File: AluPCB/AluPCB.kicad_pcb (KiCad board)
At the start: 2 copper layers, 60 x 50 mm, 78 parts, among them J1 CON_U, J2 CON_U, J3 CON_U, Q1 AON6276, Q2 AON6276, Q3 AON6276, Q4 AON6276, Q5 AON6276, Q6 AON6276

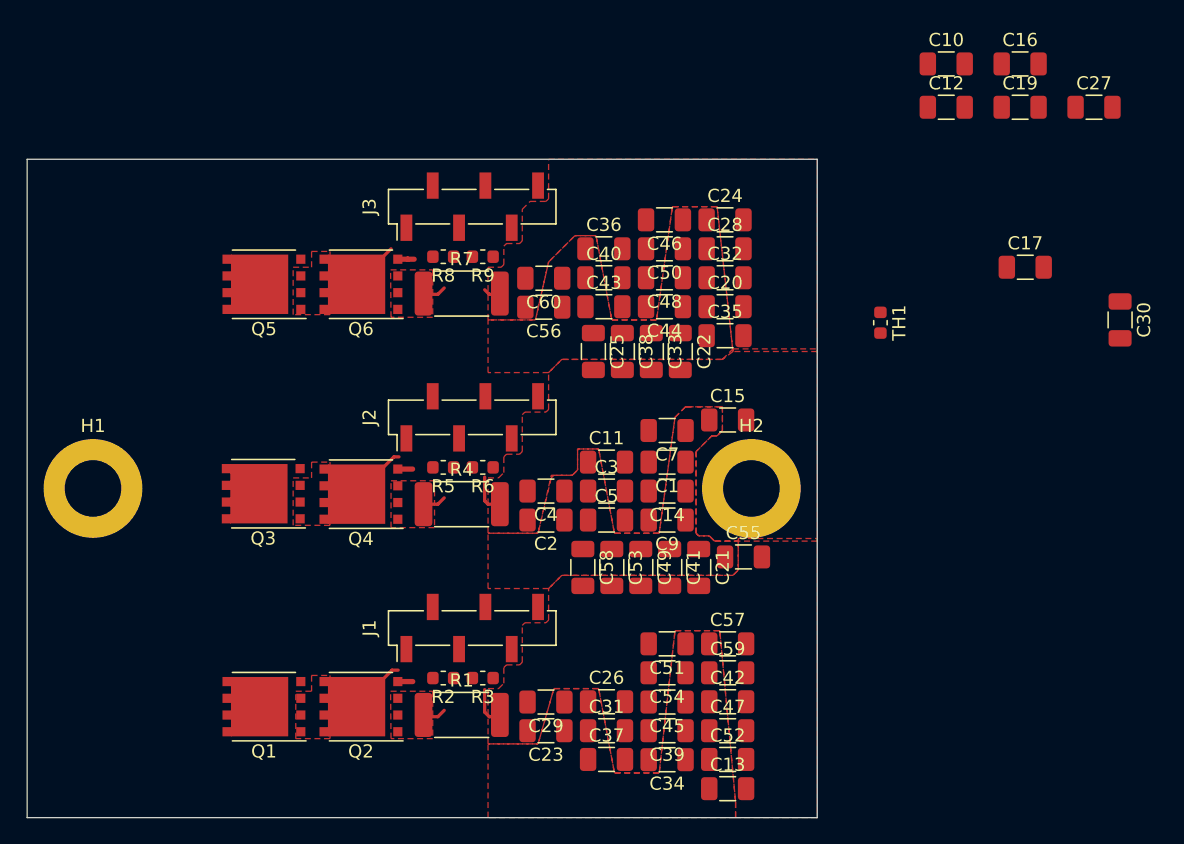
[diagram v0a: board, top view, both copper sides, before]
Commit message: finished AluPCB Power Stage 1, added images
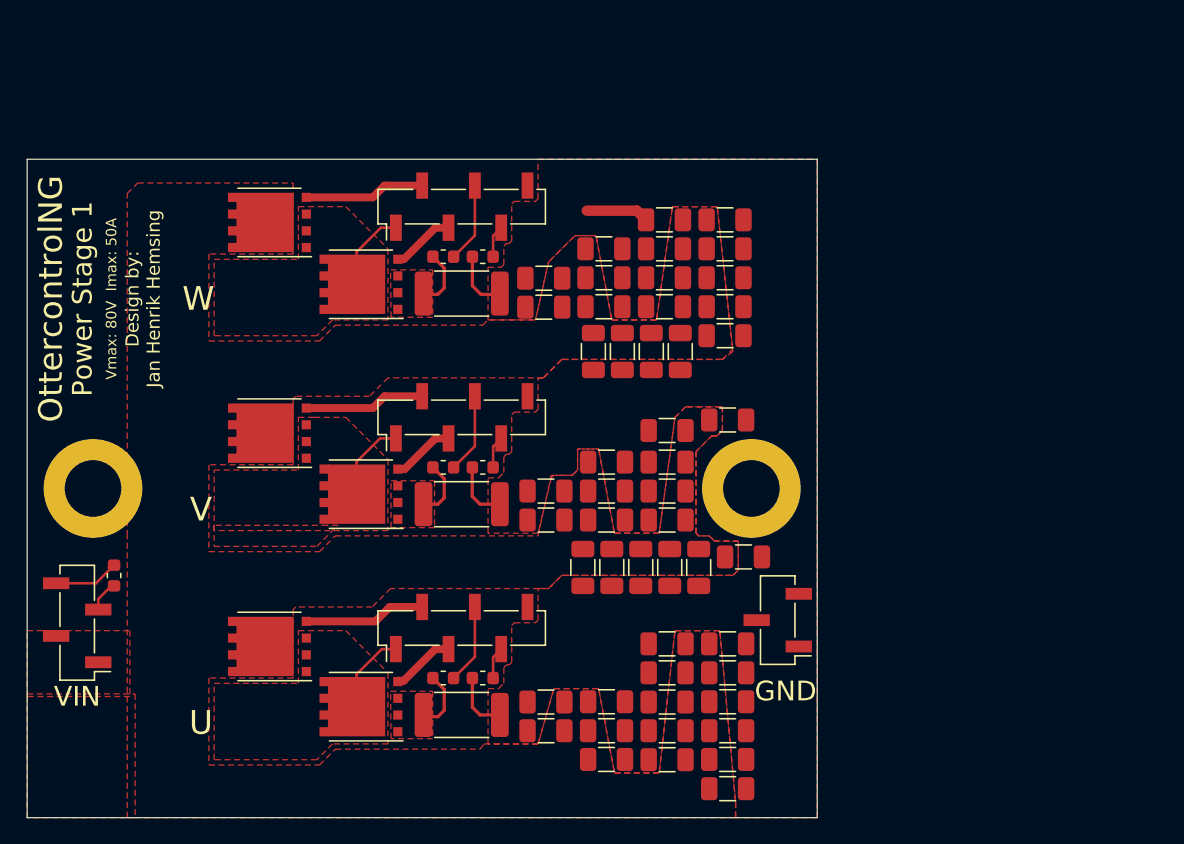
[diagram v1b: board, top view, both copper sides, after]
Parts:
- removed C10, C12, C16, C17, C19, C27, C30: 2u2, Capacitor_SMD:C_1206_3216Metric
- added J4: GND, Connector_PinSocket_2.00mm:PinSocket_1x03_P2.00mm_Vertical_SMD_Pin1Left, F.Cu at (77.0, 55.0)
- added J5: VIN, Connector_PinSocket_2.00mm:PinSocket_1x04_P2.00mm_Vertical_SMD_Pin1Left, F.Cu at (23.8, 55.2)
- moved TH1 61.3 mm to (26.6, 51.6)
- moved Q5 4.71 mm to (38.4, 24.8)
- moved Q3 4.62 mm to (38.4, 40.8)
- moved Q1 4.59 mm to (38.4, 57.0)
- moved J1 0.80 mm to (53.0, 55.6)
- moved J2 0.80 mm to (53.0, 39.6)
- moved J3 0.80 mm to (53.0, 23.6)
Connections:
- H1 pad 1: GND -> Net-(H1-Pad1)
- J1 pad 1: GUH -> U
- J1 pad 2: GUL -> GUH
- J1 pad 3: U -> GUL
- J1 pad 5: Net-(J1-Pad5) -> IUL
- J1 pad 6: IUL -> Net-(J1-Pad6)
- J2 pad 1: GVH -> V
- J2 pad 2: GVL -> GVH
- J2 pad 3: V -> GVL
- J2 pad 5: Net-(J2-Pad5) -> IVL
- J2 pad 6: IVL -> Net-(J2-Pad6)
- J3 pad 1: GWH -> W
- J3 pad 2: GWL -> GWH
- J3 pad 3: W -> GWL
- J3 pad 5: Net-(J3-Pad5) -> IWL
- J3 pad 6: IWL -> Net-(J3-Pad6)
- TH1 pad 1: Net-(J3-Pad5) -> Net-(J5-Pad4)
- TH1 pad 2: Net-(J2-Pad5) -> Net-(J5-Pad3)
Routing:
- net GND: track 7.27 -> 18.5 mm
- net GUH: track 0.00 -> 9.25 mm
- net GVH: track 0.00 -> 9.17 mm
- net GWH: track 0.00 -> 9.17 mm
- net IWH: track 0.00 -> 6.07 mm
- net IVH: track 0.00 -> 6.07 mm
- net IUH: track 0.00 -> 6.07 mm
- net Net-(J5-Pad4): track 0.00 -> 5.37 mm
- net GUL: track 1.14 -> 4.87 mm
- net GVL: track 1.12 -> 4.82 mm
- net GWL: track 1.26 -> 4.84 mm
- net W: track 3.78 -> 6.75 mm
- net Net-(Q2-Pad1): track 1.80 -> 4.61 mm
- net Net-(Q6-Pad1): track 1.80 -> 4.54 mm
- net Net-(Q4-Pad1): track 1.80 -> 4.47 mm
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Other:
- net class HV added: clearance 0.4, trace_width 0.25, via_dia 0.8, via_drill 0.4
- board text added: "Design by: Jan Henrik Hemsing"
- board text added: "GND"
- board text added: "OttercontrolNG"
- board text added: "Power Stage 1"
- board text added: "U"
- board text added: "V"
- board text added: "VIN"
- board text added: "Vmax: 80V Imax: 50A"
- board text added: "W"

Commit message: wip
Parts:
- removed C4: 2u2, Capacitor_SMD:C_1206_3216Metric
- J5: footprint Connector_PinSocket_2.00mm:PinSocket_1x04_P2.00mm_Vertical_SMD_Pin1Left -> Connector_PinSocket_2.00mm:PinSocket_1x03_P2.00mm_Vertical_SMD_Pin1Left
- moved C15 2.58 mm to (70.7, 39.1), turned to 90 degrees
- moved TH1 2.25 mm to (26.2, 53.8), turned to 90 degrees
- moved C2 1.39 mm to (58.1, 48.0), turned to 90 degrees
- moved C1 1.30 mm to (67.3, 43.0)
- moved C14 1.30 mm to (67.3, 45.2)
- moved C9 1.30 mm to (67.3, 47.4)
- moved C3 1.30 mm to (62.7, 45.2)
- moved C5 1.30 mm to (62.7, 47.4)
- moved C11 1.30 mm to (62.7, 43.0)
- moved C7 1.30 mm to (67.3, 40.6)
- moved H1 1.25 mm to (26.2, 45.0)
- moved H2 1.25 mm to (73.8, 45.0)
- moved J5 1.00 mm to (23.8, 56.2), turned to 0 degrees
- moved C55 0.22 mm to (74.4, 50.4)
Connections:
- J5 pad 1: VIN -> Net-(J5-Pad1)
- J5 pad 2: VIN -> Net-(J5-Pad2)
- J5 pad 3: Net-(J5-Pad3) -> VIN
- TH1 pad 1: Net-(J5-Pad4) -> Net-(J5-Pad2)
- TH1 pad 2: Net-(J5-Pad3) -> Net-(J5-Pad1)
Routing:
- net Net-(J5-Pad4): track 5.37 -> 0.00 mm
- net Net-(J5-Pad1): track 0.00 -> 4.54 mm
- net Net-(J5-Pad3): track 2.34 -> 0.00 mm
- net Net-(J5-Pad2): track 0.00 -> 1.94 mm

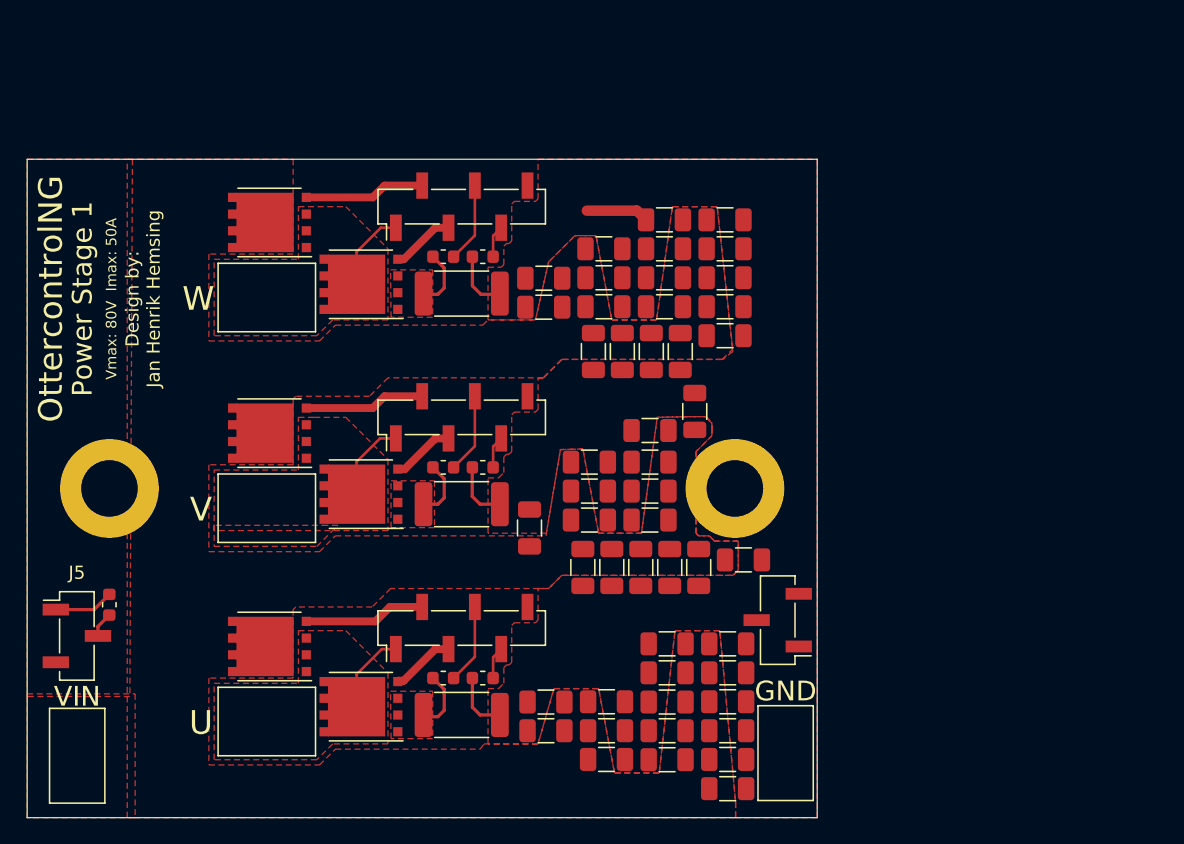
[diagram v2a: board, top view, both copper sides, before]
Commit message: updated PCB, changed size to 44x50mm
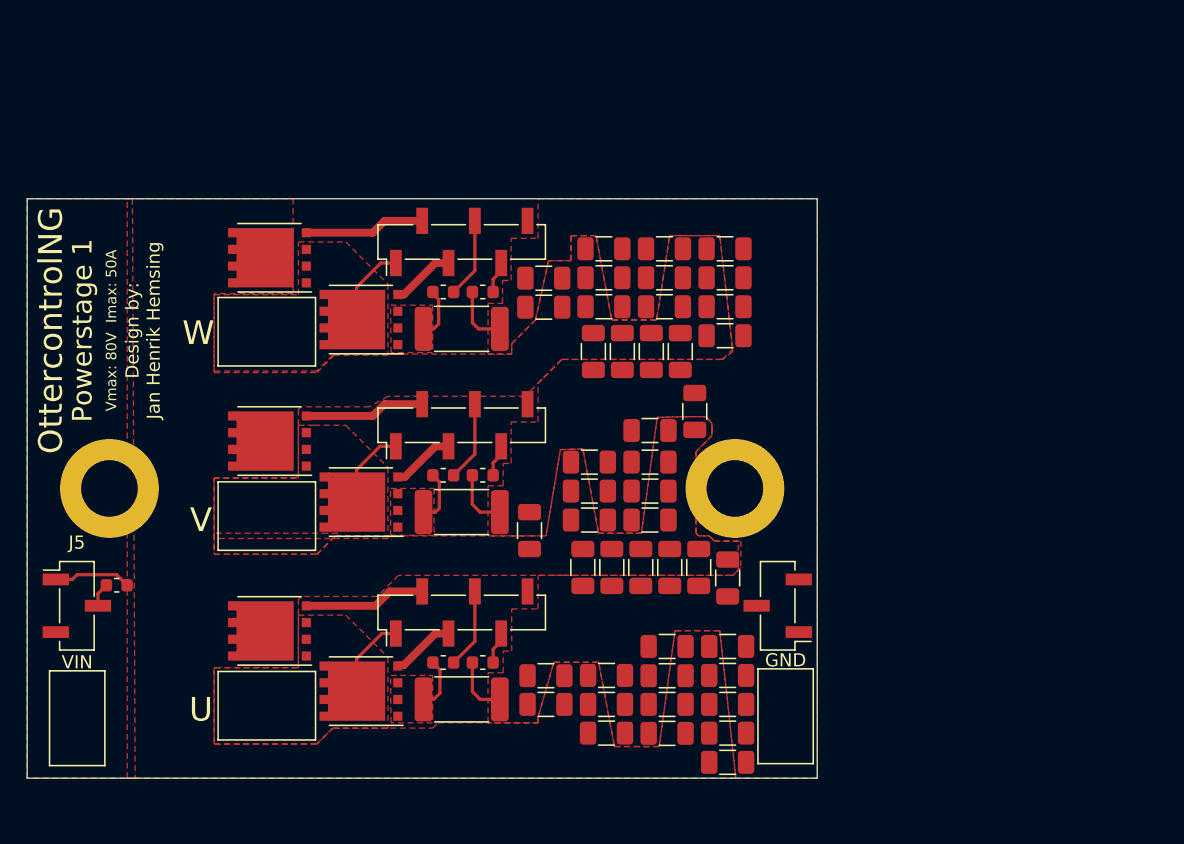
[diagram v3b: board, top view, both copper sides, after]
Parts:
- removed C24, C46, C51, C57: 2u2, Capacitor_SMD:C_1206_3216Metric
- moved J3 2.68 mm to (53.0, 26.3)
- moved Q5 2.68 mm to (38.4, 27.5)
- moved R7 2.68 mm to (53.0, 32.9)
- moved R8 2.68 mm to (51.6, 30.1)
- moved R9 2.68 mm to (54.6, 30.1)
- moved Q6 2.68 mm to (45.3, 32.2)
- moved J5 2.29 mm to (23.8, 53.9)
- moved C13 2.00 mm to (73.2, 65.8)
- moved C23 2.00 mm to (59.4, 61.4)
- moved C26 2.00 mm to (64.0, 59.2)
- moved C29 2.00 mm to (59.4, 59.2)
- moved C31 2.00 mm to (64.0, 61.4)
- moved C37 2.00 mm to (64.0, 63.6)
- moved C39 2.00 mm to (68.6, 61.4)
- moved C42 2.00 mm to (73.2, 59.2)
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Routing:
- net GND: track 18.5 -> 13.8 mm
- net Net-(J5-Pad1): track 4.54 -> 5.89 mm
- net Net-(Q6-Pad1): track 4.54 -> 3.91 mm
- net Net-(Q2-Pad1): track 4.61 -> 3.99 mm
- net IVL: track 2.45 -> 3.05 mm
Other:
- board size 60 x 50 mm -> 60 x 44 mm
- board text added: "Powerstage 1"
- board text removed: "Power Stage 1"

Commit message: finished ALUpcb
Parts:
- moved C55 13.4 mm to (68.0, 39.5), turned to 90 degrees
- moved C15 4.96 mm to (65.8, 39.5)
- moved C7 4.00 mm to (63.5, 39.5), turned to 90 degrees
- moved C21 1.15 mm to (71.0, 52.1)
- moved C1 1.10 mm to (66.2, 42.9), turned to 0 degrees
- moved C11 1.10 mm to (61.6, 42.9), turned to 180 degrees
- moved C14 1.10 mm to (66.2, 45.1), turned to 0 degrees
- moved C3 1.10 mm to (61.6, 45.1), turned to 180 degrees
- moved C9 1.10 mm to (66.2, 47.4), turned to 0 degrees
- moved C5 1.10 mm to (61.6, 47.4), turned to 180 degrees
- moved C41 0.50 mm to (68.8, 51.5)

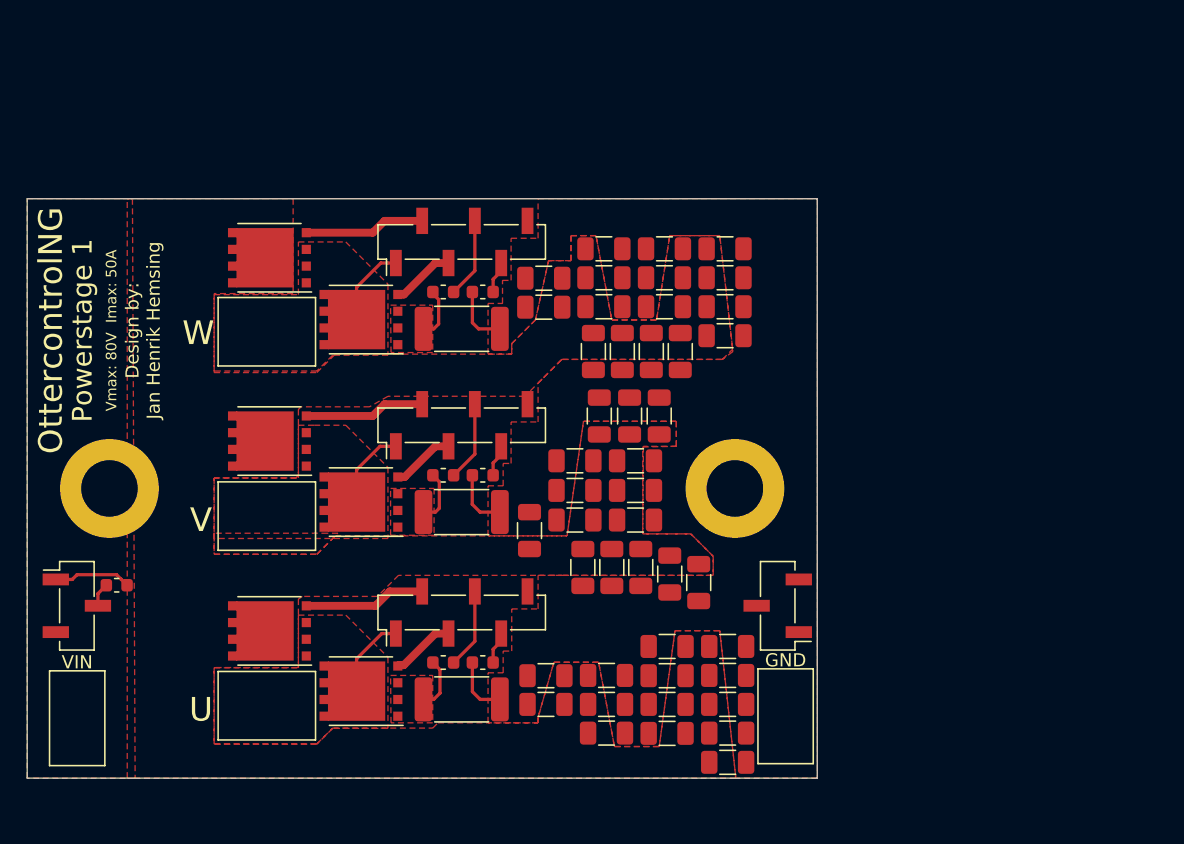
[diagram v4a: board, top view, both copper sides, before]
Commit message: finalized Powerstage, ordered PCBs
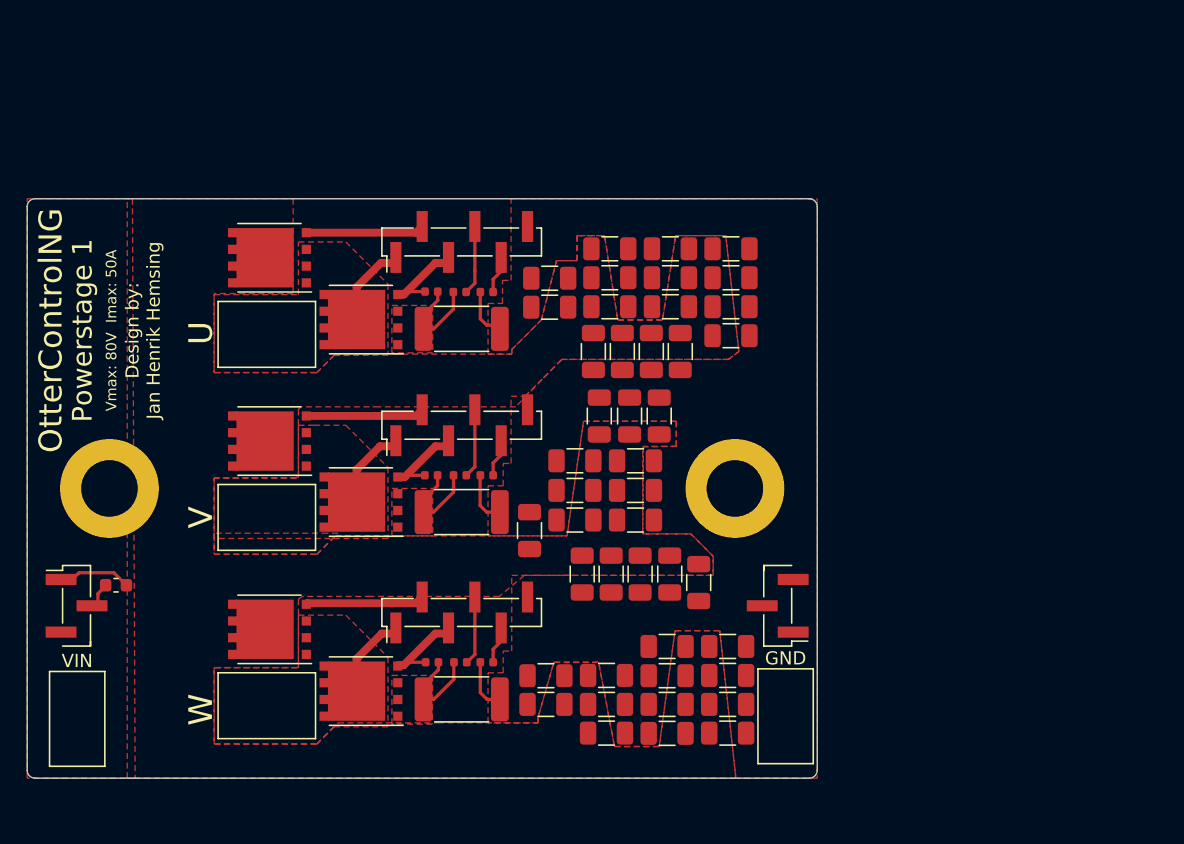
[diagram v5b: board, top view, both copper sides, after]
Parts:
- removed C13: 2u2, Capacitor_SMD:C_1206_3216Metric
- added R10: 10k, Resistor_SMD:R_0402_1005Metric, F.Cu at (50.8, 58.2)
- added R11: 10k, Resistor_SMD:R_0402_1005Metric, F.Cu at (50.7, 44.0)
- added R12: 10k, Resistor_SMD:R_0402_1005Metric, F.Cu at (50.7, 30.1)
- J1, J2, J3: footprint Connector_PinSocket_2.00mm:PinSocket_1x06_P2.00mm_Vertical_SMD_Pin1Left -> Connector_PinHeader_2.00mm:PinHeader_1x06_P2.00mm_Vertical_SMD_Pin1Left
- J4, J5: footprint Connector_PinSocket_2.00mm:PinSocket_1x03_P2.00mm_Vertical_SMD_Pin1Left -> Connector_PinHeader_2.00mm:PinHeader_1x03_P2.00mm_Vertical_SMD_Pin1Left
- R2, R3, R5, R6, R8, R9: footprint Resistor_SMD:R_0603_1608Metric -> Resistor_SMD:R_0402_1005Metric
- moved R2 1.30 mm to (52.9, 58.2)
- moved R5 1.27 mm to (52.9, 44.0)
- moved R8 1.25 mm to (52.9, 30.1)
- moved C53 0.50 mm to (64.3, 51.5)
- moved C58 0.50 mm to (62.1, 51.5)
- moved C49 0.50 mm to (66.5, 51.5)
- moved C20 0.45 mm to (73.5, 31.2)
- moved C28 0.45 mm to (73.5, 26.8)
- moved C32 0.45 mm to (73.5, 29.0)
- moved C35 0.45 mm to (73.5, 33.4)
- moved C36 0.45 mm to (64.2, 26.8)
- moved C40 0.45 mm to (64.2, 29.0)
- moved C43 0.45 mm to (64.2, 31.2)
- moved C50 0.45 mm to (68.9, 26.8)
- moved C56 0.45 mm to (59.7, 31.2)
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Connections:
- J1 pad 6: Net-(J1-Pad6) -> GND
- J2 pad 6: Net-(J2-Pad6) -> GND
- J3 pad 6: Net-(J3-Pad6) -> GND
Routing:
- net Net-(Q6-Pad1): track 3.91 -> 7.47 mm
- net Net-(Q2-Pad1): track 3.99 -> 7.50 mm
- net Net-(Q4-Pad1): track 4.06 -> 7.46 mm
- net GWL: track 4.84 -> 7.00 mm
- net GVL: track 4.82 -> 6.92 mm
- net GND: track 13.8 -> 11.9 mm
- net GUL: track 4.87 -> 6.63 mm
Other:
- outline, holes or cut-outs redrawn
- board text added: "OtterControlNG"
- board text removed: "OttercontrolNG"
